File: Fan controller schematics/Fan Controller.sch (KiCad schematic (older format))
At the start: 10 parts, among them IC1 ATMEGA328-P, SW1 ROTARY_ENCODER, U1 LM385-1.25, Y1 16MHz

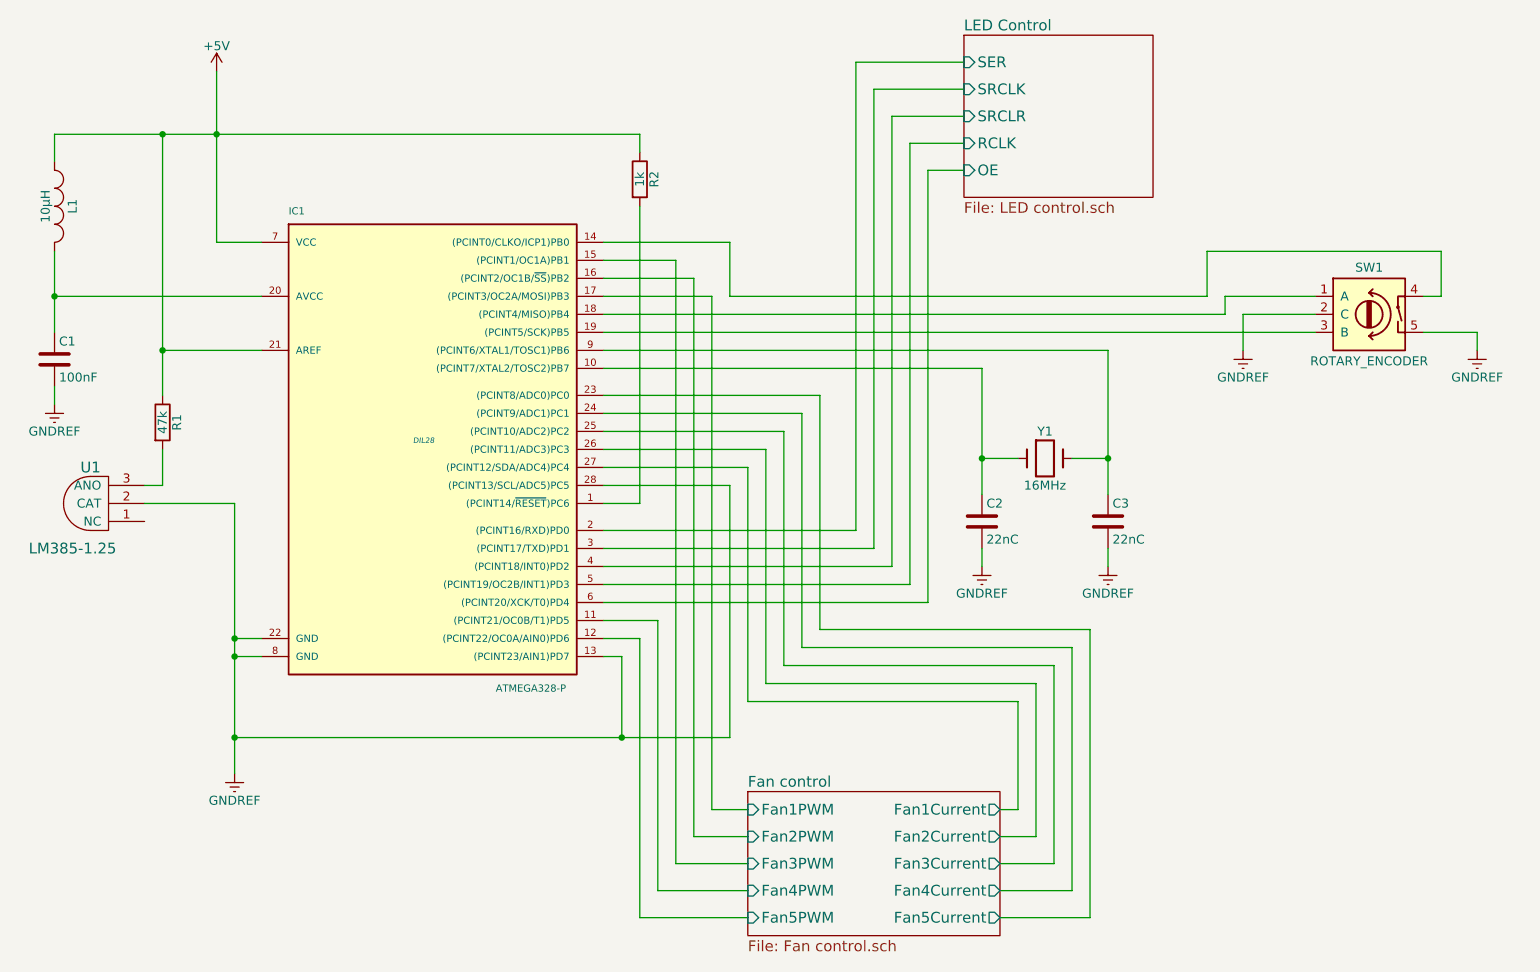
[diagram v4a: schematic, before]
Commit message: Add cap to AREF
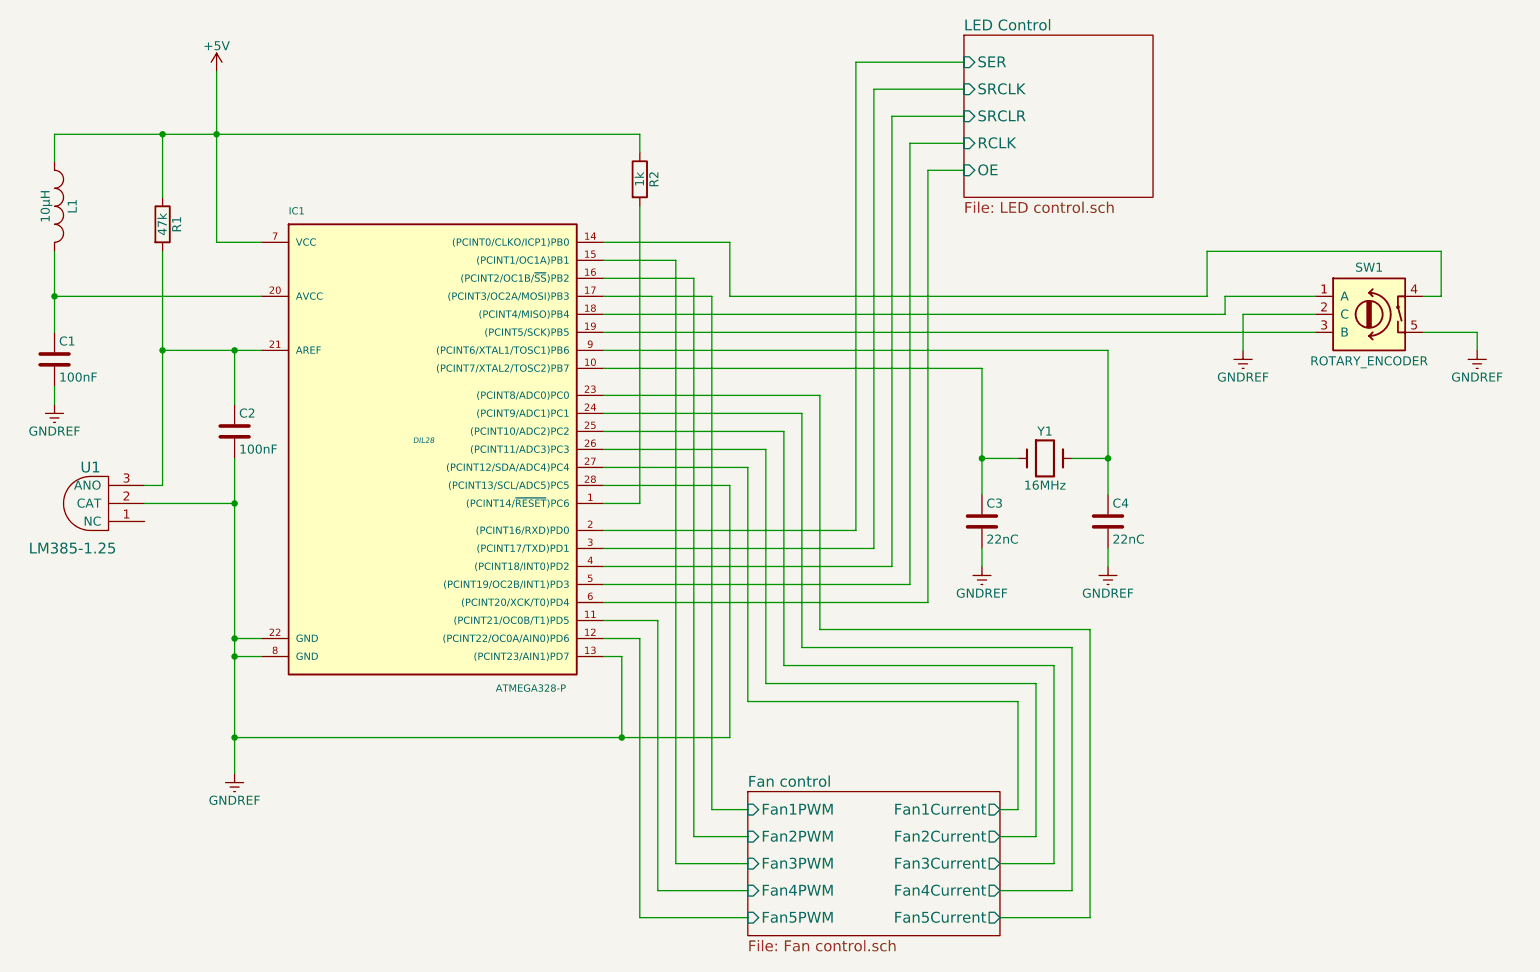
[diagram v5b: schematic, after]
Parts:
- added C2: 100nF, symbol C
- renumbered C2 to C3, C3 to C4
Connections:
- net +5V: no longer IC1.21 (AREF)
- net GNDREF: now also C2.2
- net at R1.2, U1.3 (ANO): now also IC1.21 (AREF), C2.1
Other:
- moved on the sheet: R1
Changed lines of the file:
@@
 $EndComp
 $Comp
-L C C2
+L C C3
 U 1 1 57DB00C1
 P 6000 4350
-F 0 "C2" H 6025 4450 50  0000 L CNN
+F 0 "C3" H 6025 4450 50  0000 L CNN
 F 1 "22nC" H 6025 4250 50  0000 L CNN
 F 2 "" H 6038 4200 50  0000 C CNN
@@
 $EndComp
 $Comp
-L C C3
+L C C4
 U 1 1 57DB0741
 P 6700 4350
-F 0 "C3" H 6725 4450 50  0000 L CNN
+F 0 "C4" H 6725 4450 50  0000 L CNN
 F 1 "22nC" H 6725 4250 50  0000 L CNN
 F 2 "" H 6738 4200 50  0000 C CNN
@@
 	2000 5000 1850 5000
 Wire Wire Line
-	1850 4250 1850 5750
+	1850 4000 1850 4250
+Wire Wire Line
+	1850 4250 1850 5000
+Wire Wire Line
+	1850 5000 1850 5100
+Wire Wire Line
+	1850 5100 1850 5550
+Wire Wire Line
+	1850 5550 1850 5750
 Wire Wire Line
 	2000 5100 1850 5100
@@
 	850  3100 2000 3100
 Wire Wire Line
-	6000 3500 6000 4200
+	6000 3500 6000 4000
+Wire Wire Line
+	6000 4000 6000 4200
 Wire Wire Line
 	6000 4000 6200 4000
@@
 	6500 4000 6700 4000
 Wire Wire Line
-	6700 3400 6700 4200
+	6700 3400 6700 4000
+Wire Wire Line
+	6700 4000 6700 4200
 Wire Wire Line
 	6700 4500 6700 4600
@@
 	4100 2200 4100 2300
 Wire Wire Line
-	850  2200 4100 2200
+	850  2200 1450 2200
+Wire Wire Line
+	1450 2200 1750 2200
+Wire Wire Line
+	1750 2200 4100 2200
 Connection ~ 1750 2200
 Wire Wire Line
@@
 	3900 4150 4600 4150
 Wire Wire Line
-	4600 5550 4600 4150
-Wire Wire Line
-	1850 5550 4600 5550
+	4600 4150 4600 5550
+Wire Wire Line
+	4600 5550 4000 5550
+Wire Wire Line
+	4000 5550 1850 5550
 Connection ~ 1850 5550
 Wire Wire Line
@@
 $EndComp
 Wire Wire Line
-	850  2850 850  3300
+	850  2850 850  3100
+Wire Wire Line
+	850  3100 850  3300
 Connection ~ 850  3100
 Wire Wire Line
 	850  2350 850  2200
 Wire Wire Line
-	1750 1850 1750 2800
+	1750 1850 1750 2200
+Wire Wire Line
+	1750 2200 1750 2800
 $Comp
 L GNDREF #PWR1
@@
 L R R1
 U 1 1 57D96D6B
-P 1450 3800
-F 0 "R1" V 1530 3800 50  0000 C CNN
-F 1 "47k" V 1450 3800 50  0000 C CNN
-F 2 "" V 1380 3800 50  0000 C CNN
-F 3 "" H 1450 3800 50  0000 C CNN
-	1    1450 3800
-	1    0    0    -1
-$EndComp
-Wire Wire Line
-	1450 2200 1450 3650
+P 1450 2700
+F 0 "R1" V 1530 2700 50  0000 C CNN
+F 1 "47k" V 1450 2700 50  0000 C CNN
+F 2 "" V 1380 2700 50  0000 C CNN
+F 3 "" H 1450 2700 50  0000 C CNN
+	1    1450 2700
+	1    0    0    -1
+$EndComp
 Connection ~ 1450 2200
 Wire Wire Line
-	1450 3950 1450 4150
-Wire Wire Line
 	1450 4150 1350 4150
 Wire Wire Line
-	2000 3400 1450 3400
+	2000 3400 1850 3400
+Wire Wire Line
+	1850 3400 1450 3400
 Connection ~ 1450 3400
+$Comp
+L C C2
+U 1 1 57D9A64A
+P 1850 3850
+F 0 "C2" H 1875 3950 50  0000 L CNN
+F 1 "100nF" H 1875 3750 50  0000 L CNN
+F 2 "" H 1888 3700 50  0000 C CNN
+F 3 "" H 1850 3850 50  0000 C CNN
+	1    1850 3850
+	1    0    0    -1
+$EndComp
+Wire Wire Line
+	1450 2200 1450 2550
+Wire Wire Line
+	1450 2850 1450 3400
+Wire Wire Line
+	1450 3400 1450 4150
+Wire Wire Line
+	1850 3700 1850 3400
+Connection ~ 1850 3400
+Connection ~ 1850 4250
 $EndSCHEMATC

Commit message: Let unconnected pins float
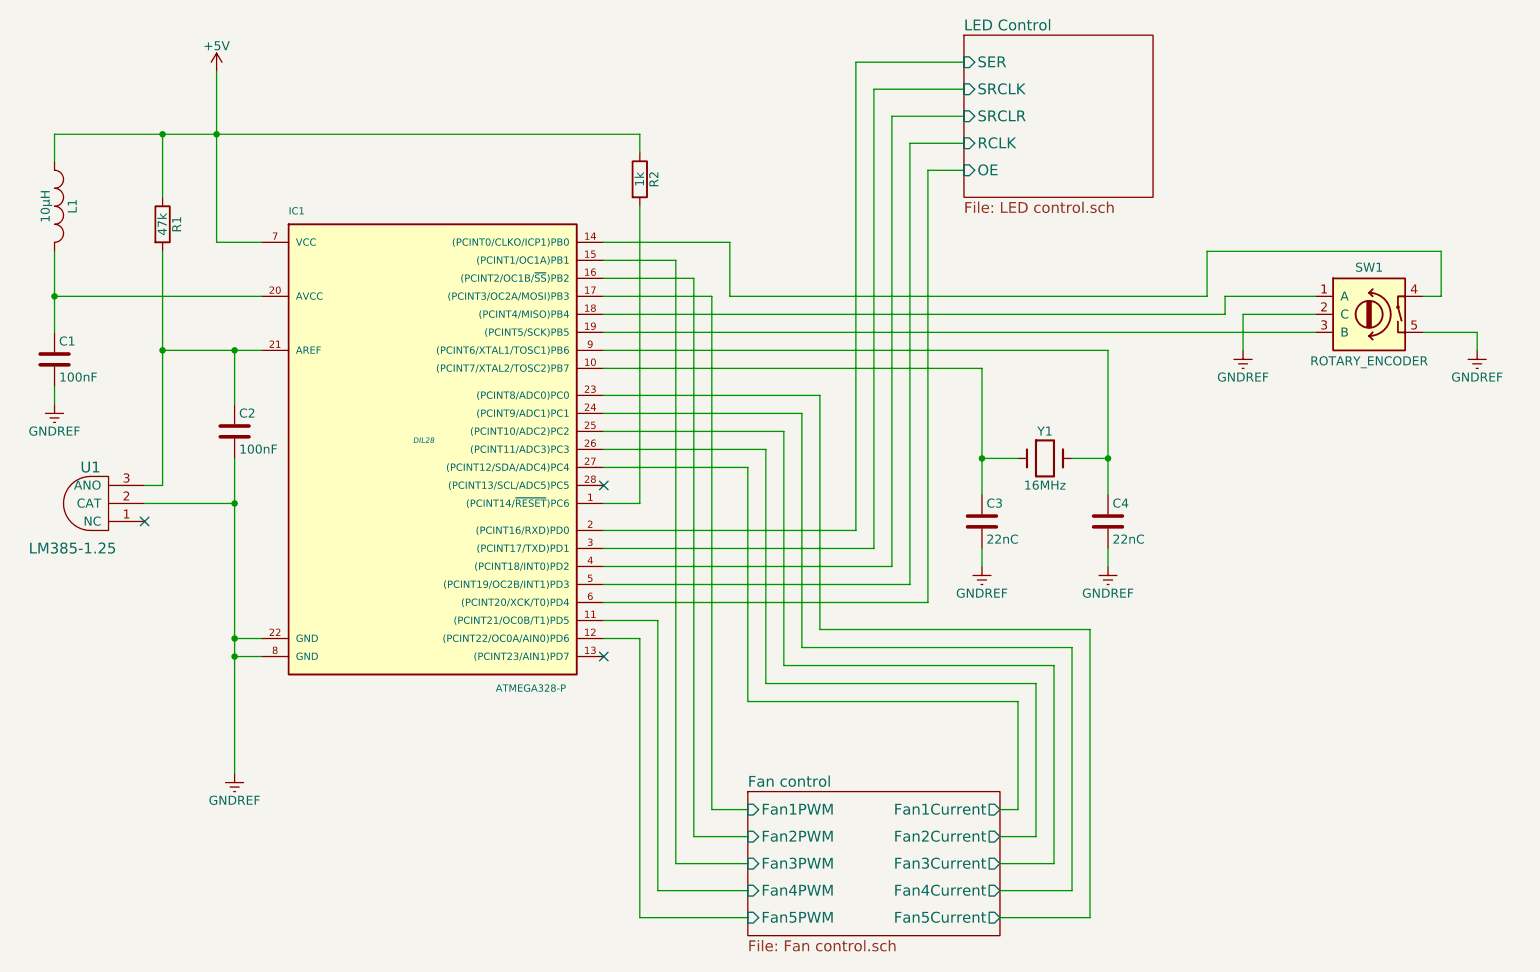
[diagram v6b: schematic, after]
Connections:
- net GNDREF: no longer IC1.13 ((PCINT23/AIN1)PD7), IC1.28 ((PCINT13/SCL/ADC5)PC5)
- no-connect marks 0 -> 3
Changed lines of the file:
@@
 	1750 2800 2000 2800
 Wire Wire Line
-	2000 5000 1850 5000
-Wire Wire Line
-	1850 4000 1850 4250
-Wire Wire Line
-	1850 4250 1850 5000
-Wire Wire Line
-	1850 5000 1850 5100
-Wire Wire Line
-	1850 5100 1850 5550
-Wire Wire Line
-	1850 5550 1850 5750
+	1850 5000 2000 5000
+Wire Wire Line
+	1850 4000 1850 5750
 Wire Wire Line
 	2000 5100 1850 5100
@@
 	850  3100 2000 3100
 Wire Wire Line
-	6000 3500 6000 4000
-Wire Wire Line
-	6000 4000 6000 4200
+	6000 3500 6000 4200
 Wire Wire Line
 	6000 4000 6200 4000
@@
 	6500 4000 6700 4000
 Wire Wire Line
-	6700 3400 6700 4000
-Wire Wire Line
-	6700 4000 6700 4200
+	6700 3400 6700 4200
 Wire Wire Line
 	6700 4500 6700 4600
@@
 	4100 2200 4100 2300
 Wire Wire Line
-	850  2200 1450 2200
-Wire Wire Line
-	1450 2200 1750 2200
-Wire Wire Line
-	1750 2200 4100 2200
+	850  2200 4100 2200
 Connection ~ 1750 2200
 Wire Wire Line
@@
 Wire Wire Line
 	4100 4250 3900 4250
-Wire Wire Line
-	3900 4150 4600 4150
-Wire Wire Line
-	4600 4150 4600 5550
-Wire Wire Line
-	4600 5550 4000 5550
-Wire Wire Line
-	4000 5550 1850 5550
-Connection ~ 1850 5550
 Wire Wire Line
 	4600 3100 7250 3100
@@
 Wire Wire Line
 	8550 3100 8450 3100
-Wire Wire Line
-	3900 5100 4000 5100
-Wire Wire Line
-	4000 5100 4000 5550
-Connection ~ 4000 5550
 $Comp
 L INDUCTOR_SMALL L1
@@
 $EndComp
 Wire Wire Line
-	850  2850 850  3100
-Wire Wire Line
-	850  3100 850  3300
+	850  2850 850  3300
 Connection ~ 850  3100
 Wire Wire Line
 	850  2350 850  2200
 Wire Wire Line
-	1750 1850 1750 2200
-Wire Wire Line
-	1750 2200 1750 2800
+	1750 1850 1750 2800
 $Comp
 L GNDREF #PWR1
@@
 	1450 4150 1350 4150
 Wire Wire Line
-	2000 3400 1850 3400
-Wire Wire Line
-	1850 3400 1450 3400
+	1450 3400 2000 3400
 Connection ~ 1450 3400
 $Comp
@@
 	1450 2200 1450 2550
 Wire Wire Line
-	1450 2850 1450 3400
-Wire Wire Line
-	1450 3400 1450 4150
+	1450 2850 1450 4150
 Wire Wire Line
 	1850 3700 1850 3400
 Connection ~ 1850 3400
 Connection ~ 1850 4250
+NoConn ~ 3900 5100
+NoConn ~ 3900 4150
+NoConn ~ 1350 4350
 $EndSCHEMATC

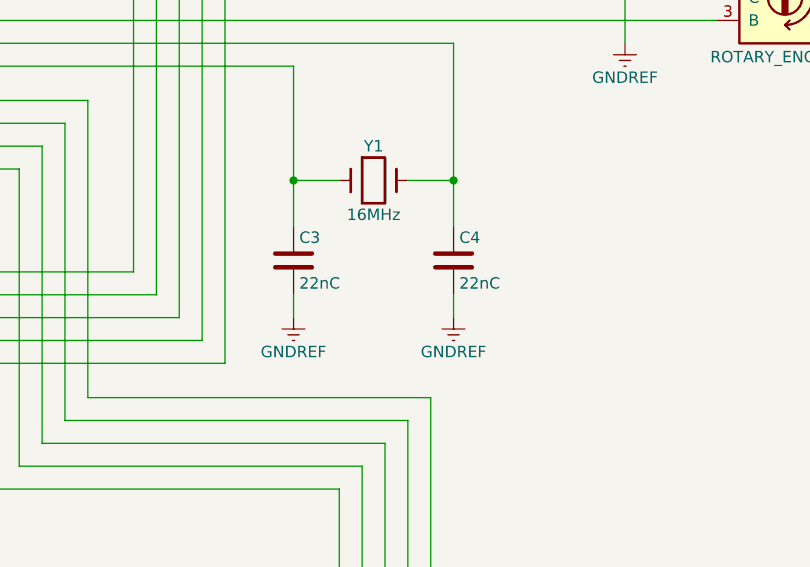
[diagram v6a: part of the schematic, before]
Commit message: Fixed wrong prefix on capacitors
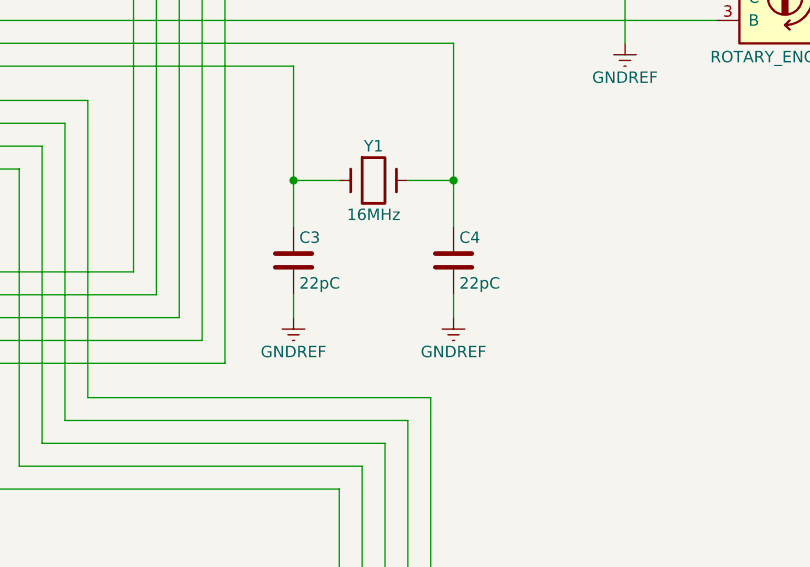
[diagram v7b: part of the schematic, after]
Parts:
- C3, C4: value 22nC -> 22pC
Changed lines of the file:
@@
 P 6000 4350
 F 0 "C3" H 6025 4450 50  0000 L CNN
-F 1 "22nC" H 6025 4250 50  0000 L CNN
+F 1 "22pC" H 6025 4250 50  0000 L CNN
 F 2 "" H 6038 4200 50  0000 C CNN
 F 3 "" H 6000 4350 50  0000 C CNN
@@
 P 6700 4350
 F 0 "C4" H 6725 4450 50  0000 L CNN
-F 1 "22nC" H 6725 4250 50  0000 L CNN
+F 1 "22pC" H 6725 4250 50  0000 L CNN
 F 2 "" H 6738 4200 50  0000 C CNN
 F 3 "" H 6700 4350 50  0000 C CNN
